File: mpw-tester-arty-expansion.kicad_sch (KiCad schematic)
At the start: 113 parts, among them J1 USB4105-GF-A, J10 61300211121, J11 61300211121, J12 61300211121, J13 61300211121, J14 61300211121, J15 61300211121, J16 61300211121, J17 61300211121, J18 61300411121, J19 61300711121, J2 61300211121, J20 61300411121, J3 Arty_A7_SPI, J4 61300211121, J5 61300311121, J6 61300211121, J7 61300211121, J8 61300211121, J9 61300211121, Q1 DTC014TEBTL, U1 SN74LVC1G125DCKR, U2 FT232HQ, U3 SN74LVC1G125DCKR, U4 MAX811REUS+T, U5 NTS0102GT, U6 MCP4661-103E/ML, U7 Caravel_breakout_PCB, U8 W25Q32FVSS, U9 MIC2211-AAYML-TR, Y1 ABM8G-12.000MHZ-18-D2Y-T, Y2 ECS-2520MVLC-100-BN-TR

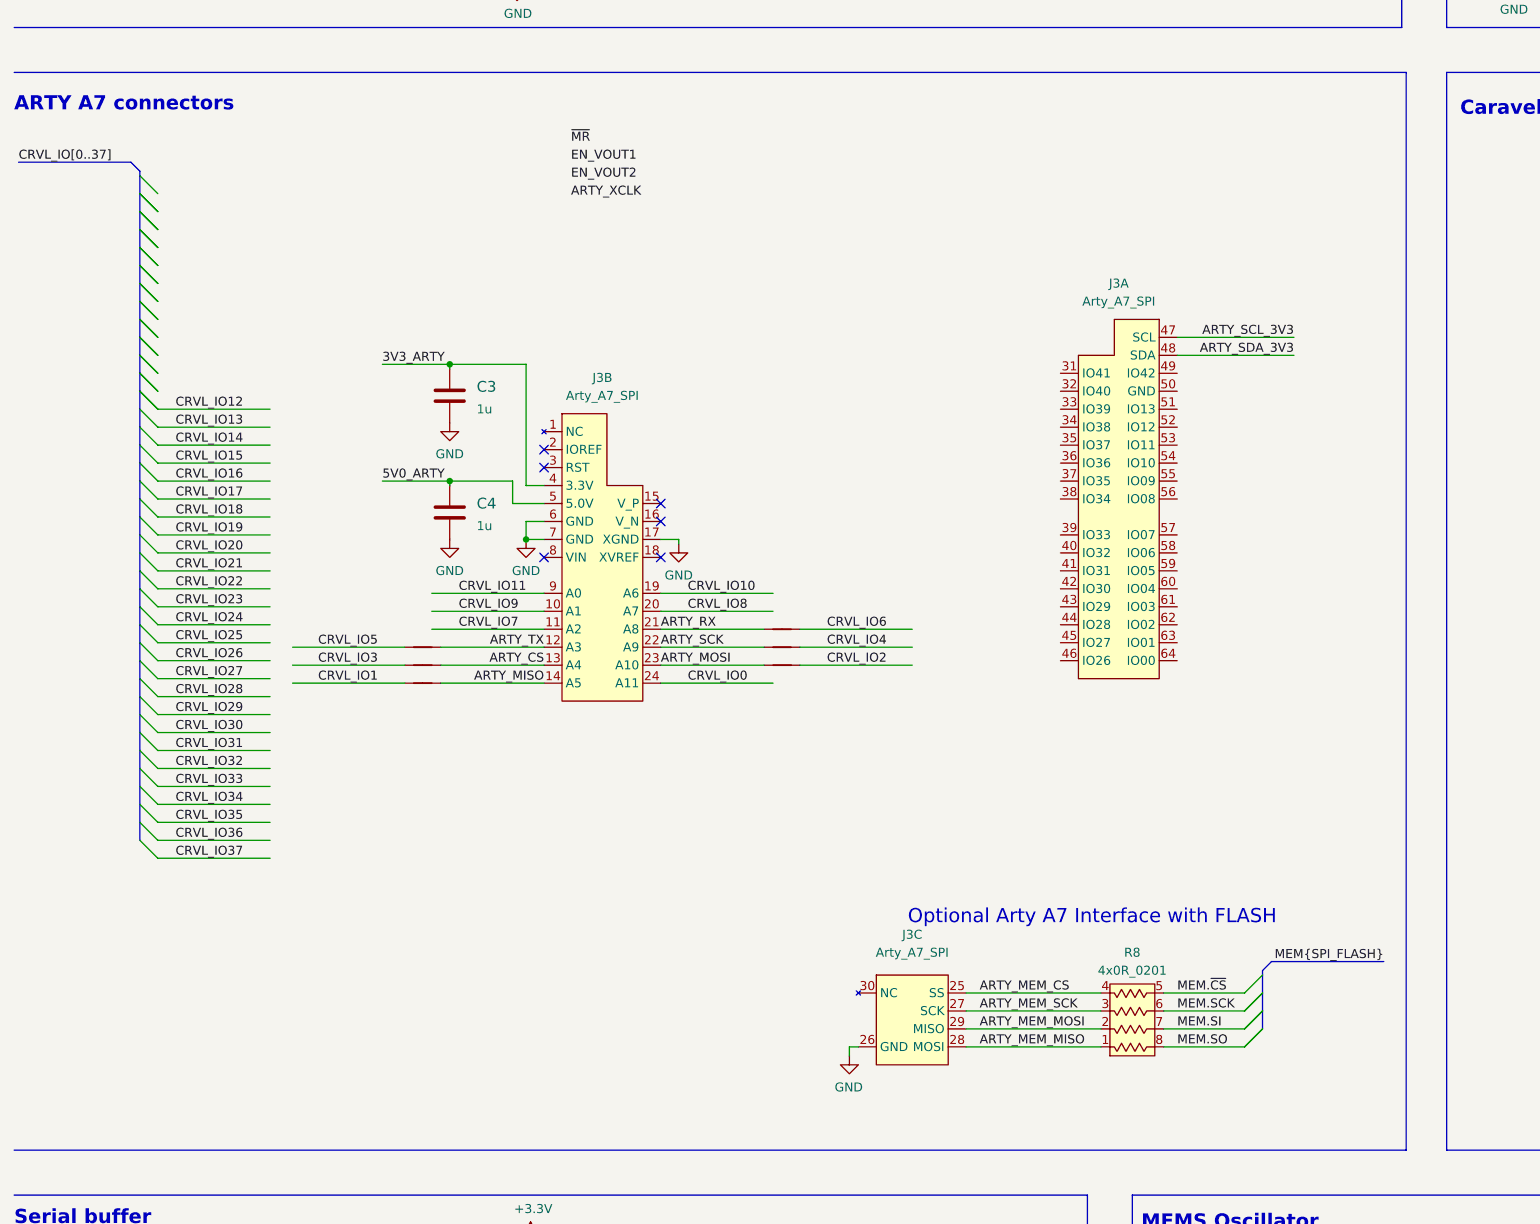
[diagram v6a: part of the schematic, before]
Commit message: Connect Caravel after rotating it on PCB. Adjust component placement
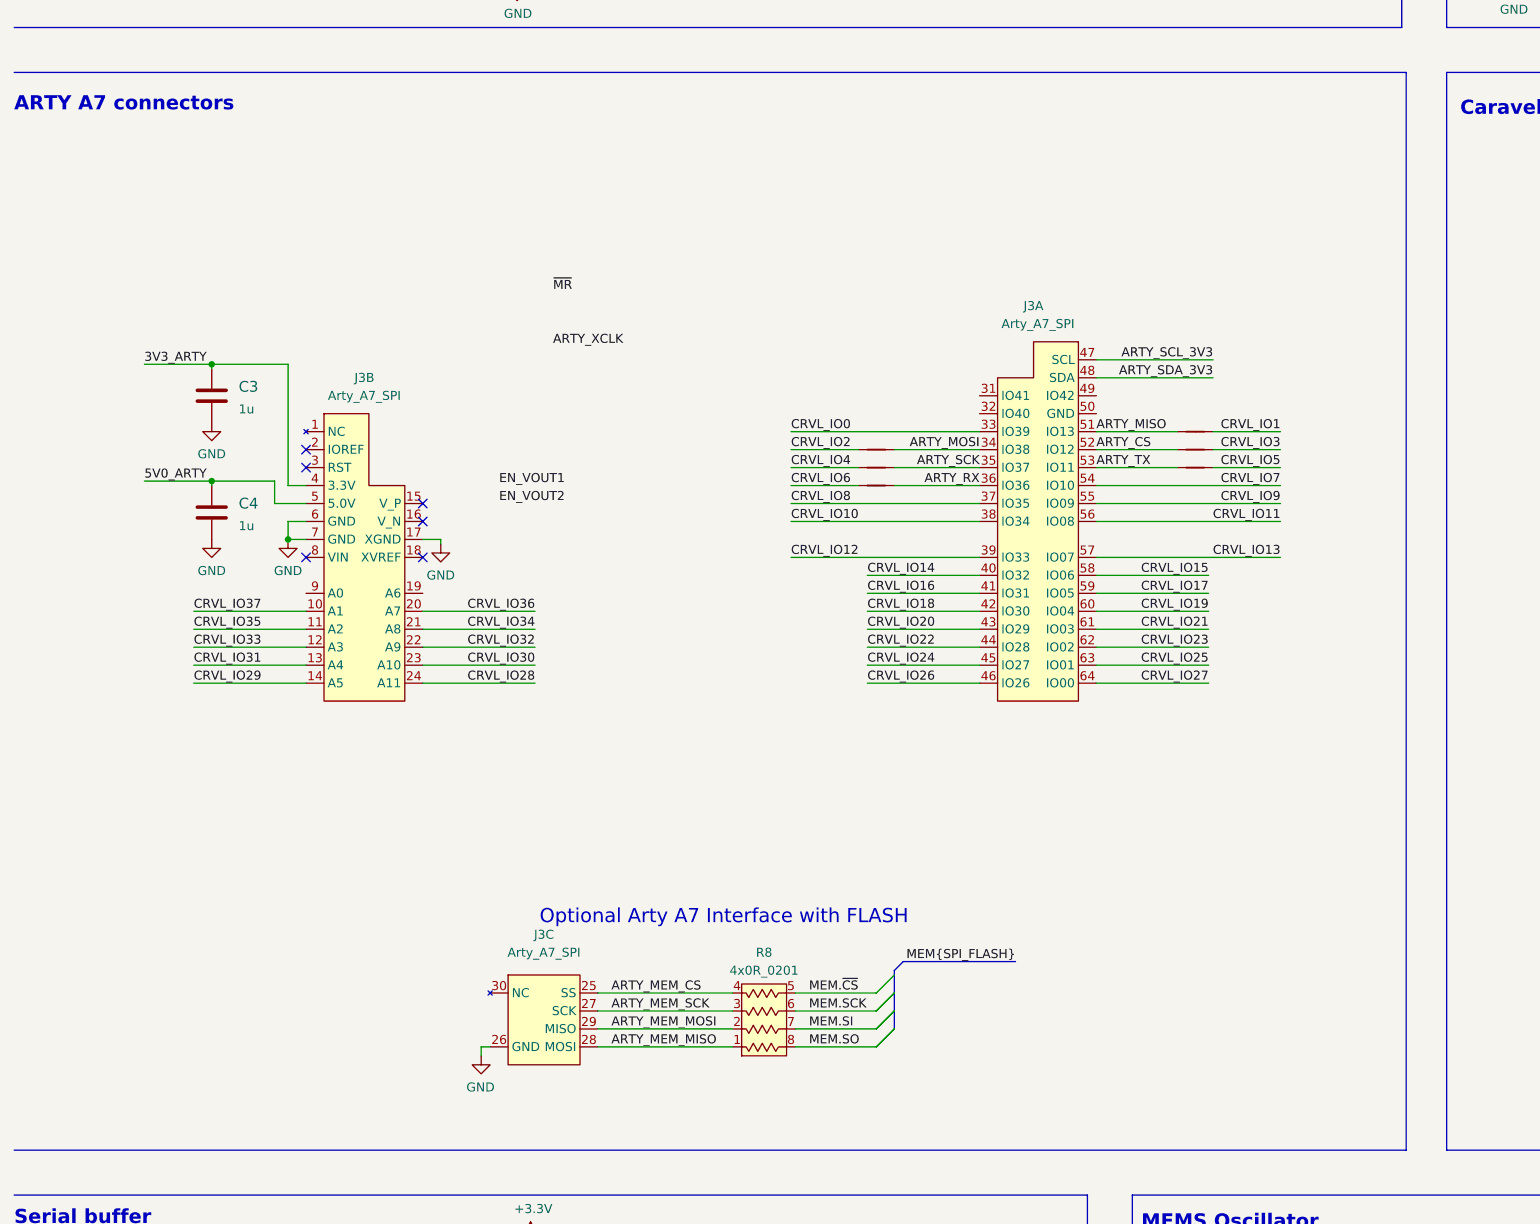
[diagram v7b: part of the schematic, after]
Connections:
- net ARTY_CS: now also J3.52 (IO12); no longer J3.13 (A4)
- net ARTY_MISO: now also J3.51 (IO13); no longer J3.14 (A5)
- net ARTY_MOSI: now also J3.34 (IO38); no longer J3.23 (A10)
- net ARTY_RX: now also J3.36 (IO36); no longer J3.21 (A8)
- net ARTY_SCK: now also J3.35 (IO37); no longer J3.22 (A9)
- net ARTY_TX: now also J3.53 (IO11); no longer J3.12 (A3)
- net CRVL_IO0: now also J3.33 (IO39); no longer J3.24 (A11)
- net CRVL_IO10: now also J3.38 (IO34); no longer J3.19 (A6)
- net CRVL_IO11: now also J3.56 (IO08); no longer J3.9 (A0)
- net CRVL_IO12: now also J3.39 (IO33)
- net CRVL_IO13: now also J3.57 (IO07)
- net CRVL_IO14: now also J3.40 (IO32)
- net CRVL_IO15: now also J3.58 (IO06)
- net CRVL_IO16: now also J3.41 (IO31)
- net CRVL_IO17: now also J3.59 (IO05)
- net CRVL_IO18: now also J3.42 (IO30)
- net CRVL_IO19: now also J3.60 (IO04)
- net CRVL_IO20: now also J3.43 (IO29)
- net CRVL_IO21: now also J3.61 (IO03)
- net CRVL_IO22: now also J3.44 (IO28)
- net CRVL_IO23: now also J3.62 (IO02)
- net CRVL_IO24: now also J3.45 (IO27)
- net CRVL_IO25: now also J3.63 (IO01)
- net CRVL_IO26: now also J3.46 (IO26)
- net CRVL_IO27: now also J3.64 (IO00)
- net CRVL_IO28: now also J3.24 (A11)
- net CRVL_IO29: now also J3.14 (A5)
- net CRVL_IO30: now also J3.23 (A10)
- net CRVL_IO31: now also J3.13 (A4)
- net CRVL_IO32: now also J3.22 (A9)
- net CRVL_IO33: now also J3.12 (A3)
- net CRVL_IO34: now also J3.21 (A8)
- net CRVL_IO35: now also J3.11 (A2)
- net CRVL_IO36: now also J3.20 (A7)
- net CRVL_IO37: now also J3.10 (A1)
- net CRVL_IO7: now also J3.54 (IO10); no longer J3.11 (A2)
- net CRVL_IO8: now also J3.37 (IO35); no longer J3.20 (A7)
- net CRVL_IO9: now also J3.55 (IO09); no longer J3.10 (A1)
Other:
- moved on the sheet: C3, C4, J3A, J3B, J3C, R8

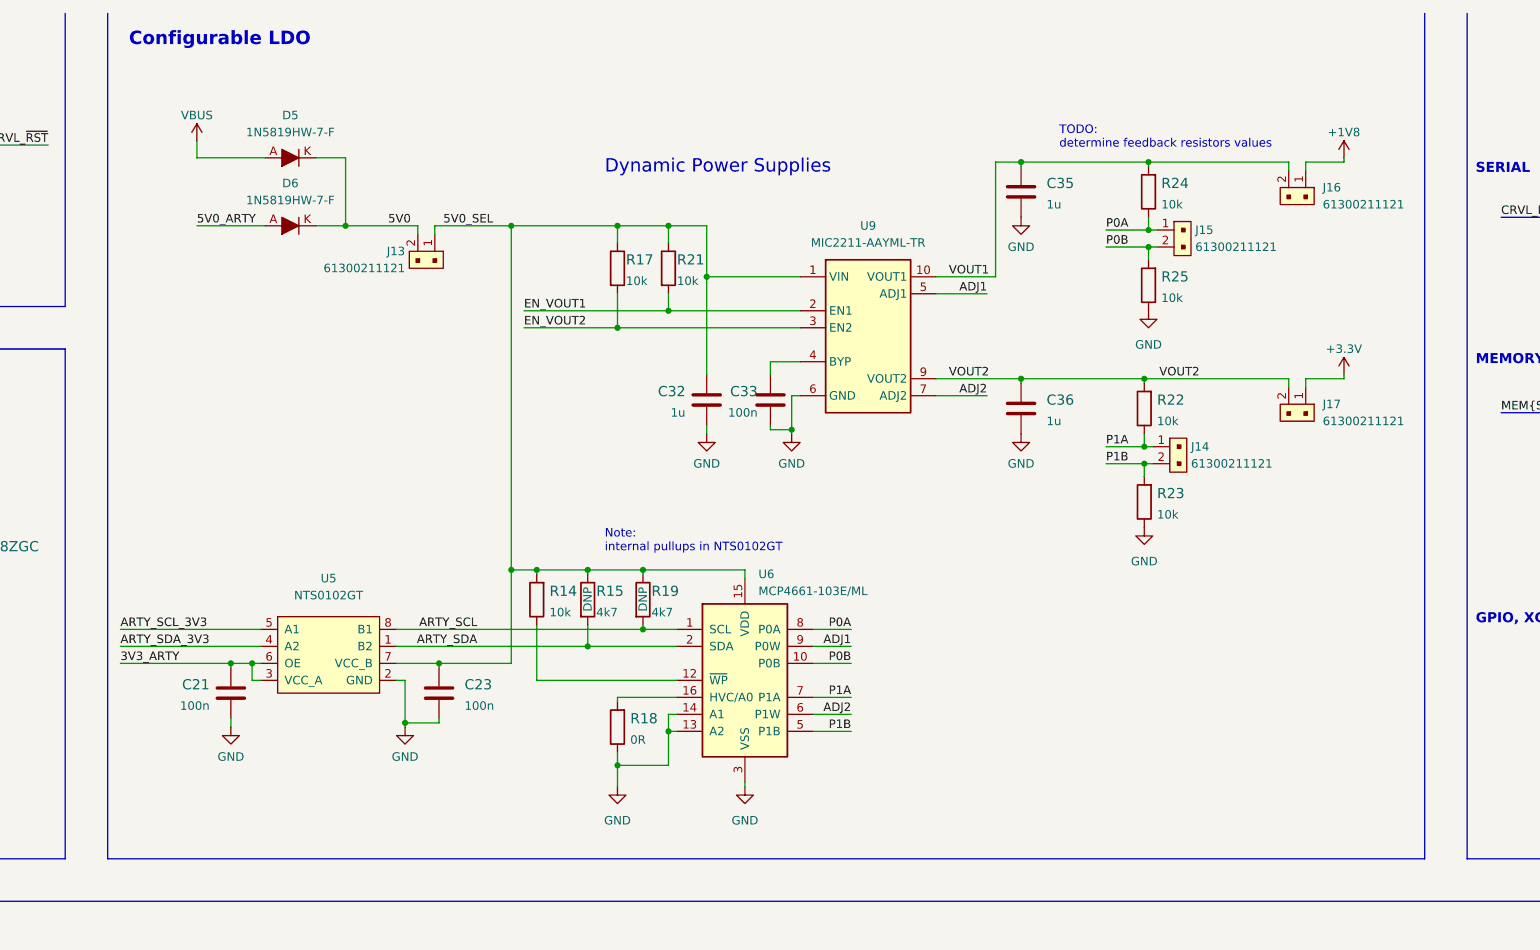
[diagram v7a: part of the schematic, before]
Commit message: Use appropriate resistor values in LDO feedback, simplify power section
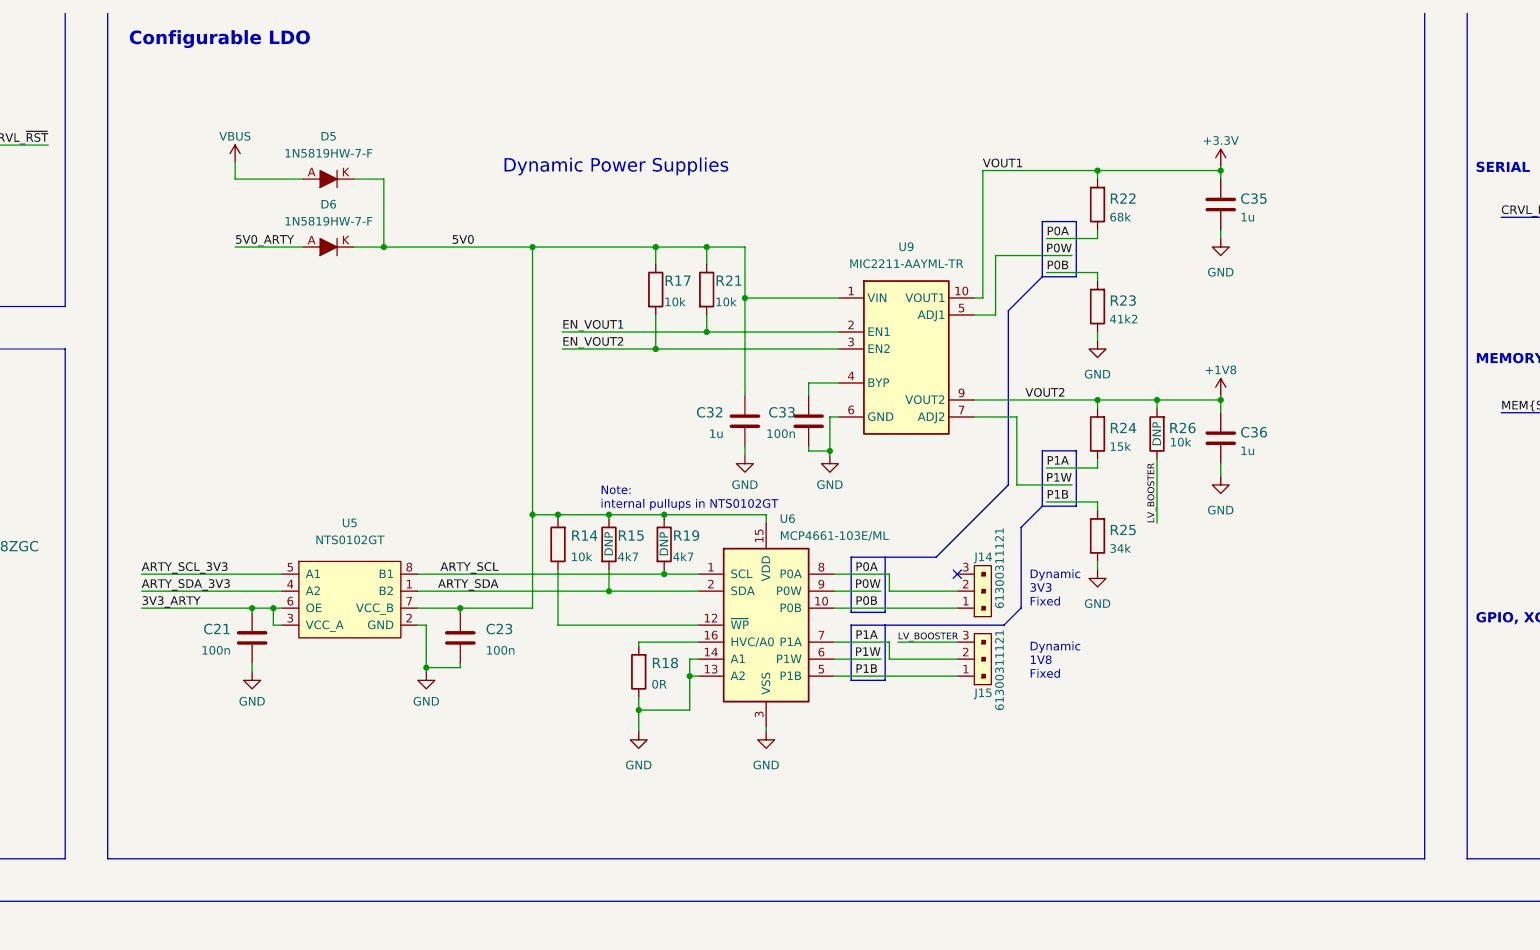
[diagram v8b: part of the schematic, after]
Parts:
- removed J13, J14, J15, J16, J17: 61300211121, antmicro-footprints:PinHeader_1x2_P2.54_Drill0.9mm, symbol antmicroRectangularConnectorsHeadersMalePins:61300211121
- removed R22, R23, R24, R25: R_10k_0402, antmicro-footprints:0402-res, symbol antmicroResistors0402:R_10k_0402
- added J14, J15: 61300311121, antmicro-footprints:PinHeader_1x3_P2.54_Drill1.1mm, symbol antmicroRectangularConnectorsHeadersMalePins:61300311121
- added R22: R_68k_0603, antmicro-footprints:0603-res, symbol antmicroResistors0603:R_68k_0603
- added R23: R_41k2_0603, antmicro-footprints:0603-res, symbol antmicroResistors0603:R_41k2_0603
- added R24: R_15k_0603, antmicro-footprints:0603-res, symbol antmicroResistors0603:R_15k_0603
- added R25: R_34k_0402, antmicro-footprints:0402-res, symbol antmicroResistors0402:R_34k_0402
- added R26: R_10k_0603, antmicro-footprints:0603-res, symbol antmicroResistors0603:R_10k_0603
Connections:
- net 5V0_SEL is gone; now on net 5V0: C23.1, C32.1, R14.2, R15.1, R17.1, R19.1, R21.1, U5.7 (VCC_B), U6.15 (VDD), U9.1 (VIN)
- net VOUT1 is gone; now on net +3V3: C35.1, U9.10 (VOUT1)
- net VOUT2 is gone; now on net +1V8: C36.1, U9.9 (VOUT2)
- net +1V8: now also R24.2, R26.2
- net +3V3: now also R22.2
- net AGND: now also R23.1, R25.1
- net P0A: now also J14.2, R22.1
- net P0B: now also J14.1, R23.2
- net P1A: now also J15.2, R24.1
- net P1B: now also J15.1, R25.2
- net ADJ1 renamed P0W
- net ADJ2 renamed P1W
- new net LV_BOOSTER: J15.3, R26.1
- no-connect marks 22 -> 23
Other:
- note added: "Dynamic 1V8 Fixed"
- note added: "Dynamic 3V3 Fixed"
- note removed: "TODO: determine feedback resistors values"
- moved on the sheet: C21, C23, C32, C33, C35, C36, D5, D6, R14, R15, R17, R18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
